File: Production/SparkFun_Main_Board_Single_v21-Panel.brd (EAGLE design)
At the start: 186.9 x 176.3 mm, 510 parts, among them J1 MICROMOD-2222-C, J10 MICRO-SD-PUSH-PUSH-EXT-PIN, J11 Vertical Qwiic Connector, J14 QWIIC_RIGHT_ANGLE, J15 MICROMOD-2222-C, J18 CORTEX_JTAG_DEBUG_MINIMUM_PTH, J2 Vertical Qwiic Connector, J20 MICRO-SD-PUSH-PUSH-EXT-PIN, J21 MICROMOD_FUNCTION_MAIN, J25 Vertical Qwiic Connector, J26 QWIIC_RIGHT_ANGLE, J27 MICROMOD-2222-C, J30 CORTEX_JTAG_DEBUG_MINIMUM_PTH, J32 MICRO-SD-PUSH-PUSH-EXT-PIN, J33 MICROMOD_FUNCTION_MAIN, J37 Vertical Qwiic Connector, J38 QWIIC_RIGHT_ANGLE, J39 MICROMOD-2222-C, J4 QWIIC_RIGHT_ANGLE, J42 CORTEX_JTAG_DEBUG_MINIMUM_PTH, J44 MICRO-SD-PUSH-PUSH-EXT-PIN, J45 MICROMOD_FUNCTION_MAIN, J5 CORTEX_JTAG_DEBUG_MINIMUM_PTH, J6 MICROMOD_FUNCTION_MAIN, Q1 3.1A/30V/105mΩ, Q2 20V/4.2A/52mΩ/1.4W, Q3 3.1A/30V/105mΩ, Q4 20V/4.2A/52mΩ/1.4W, Q5 3.1A/30V/105mΩ, Q6 20V/4.2A/52mΩ/1.4W, Q7 3.1A/30V/105mΩ, Q8 20V/4.2A/52mΩ/1.4W, U1 STG3856QTR, U10 AP7347DQ-33W5-7K-3.3V, U11 MCP73831, U12 AP7361C-33, U13 STG3856QTR, U14 ESD Diode, U15 AP7347DQ-33W5-7K-3.3V, U16 MCP73831, U17 AP7361C-33, U18 STG3856QTR, U19 ESD Diode, U2 MCP73831, U20 AP7347DQ-33W5-7K-3.3V, U3 ESD Diode, U4 AP7347DQ-33W5-7K-3.3V, U5 AP7361C-33, U6 MCP73831, U7 AP7361C-33, U8 STG3856QTR, U9 ESD Diode

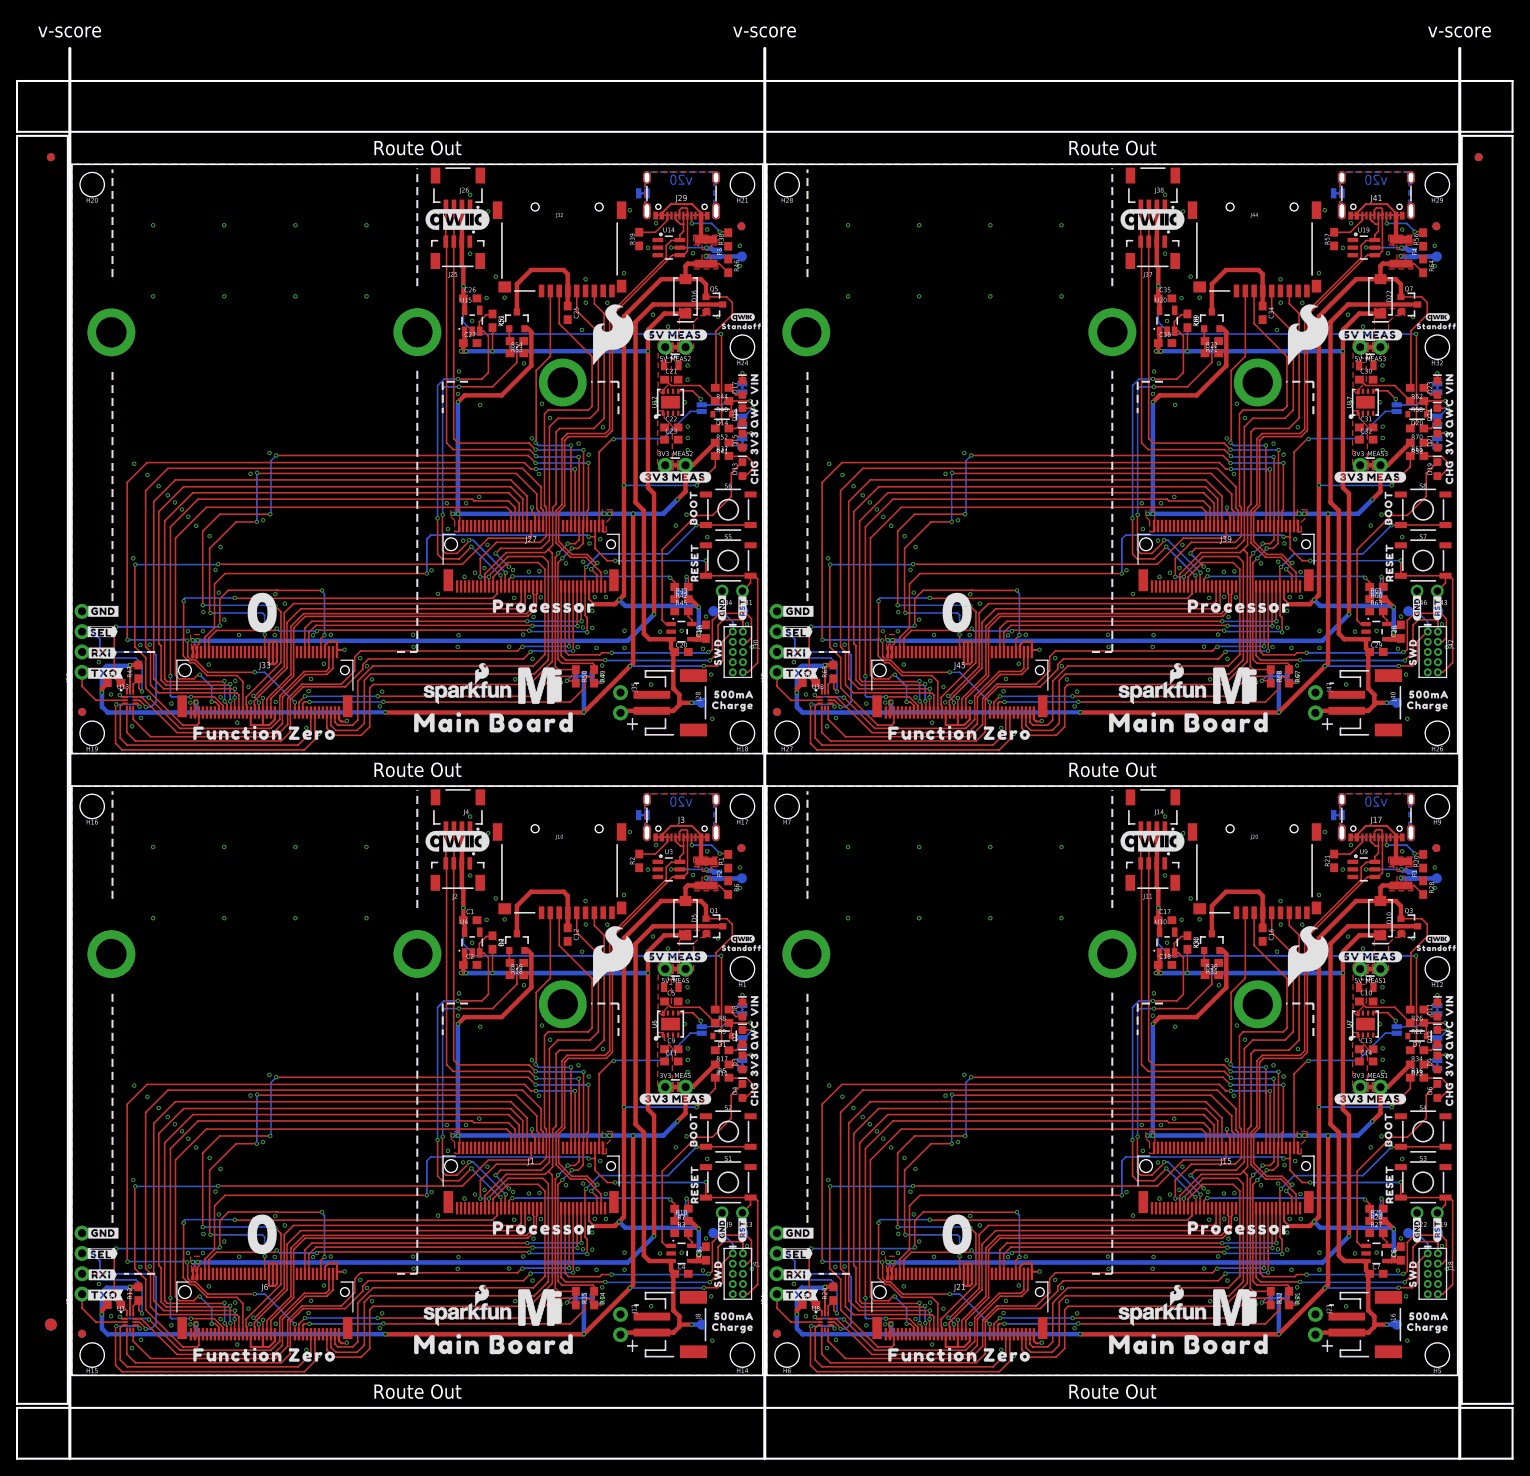
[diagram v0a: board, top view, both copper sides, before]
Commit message: Adds new production files
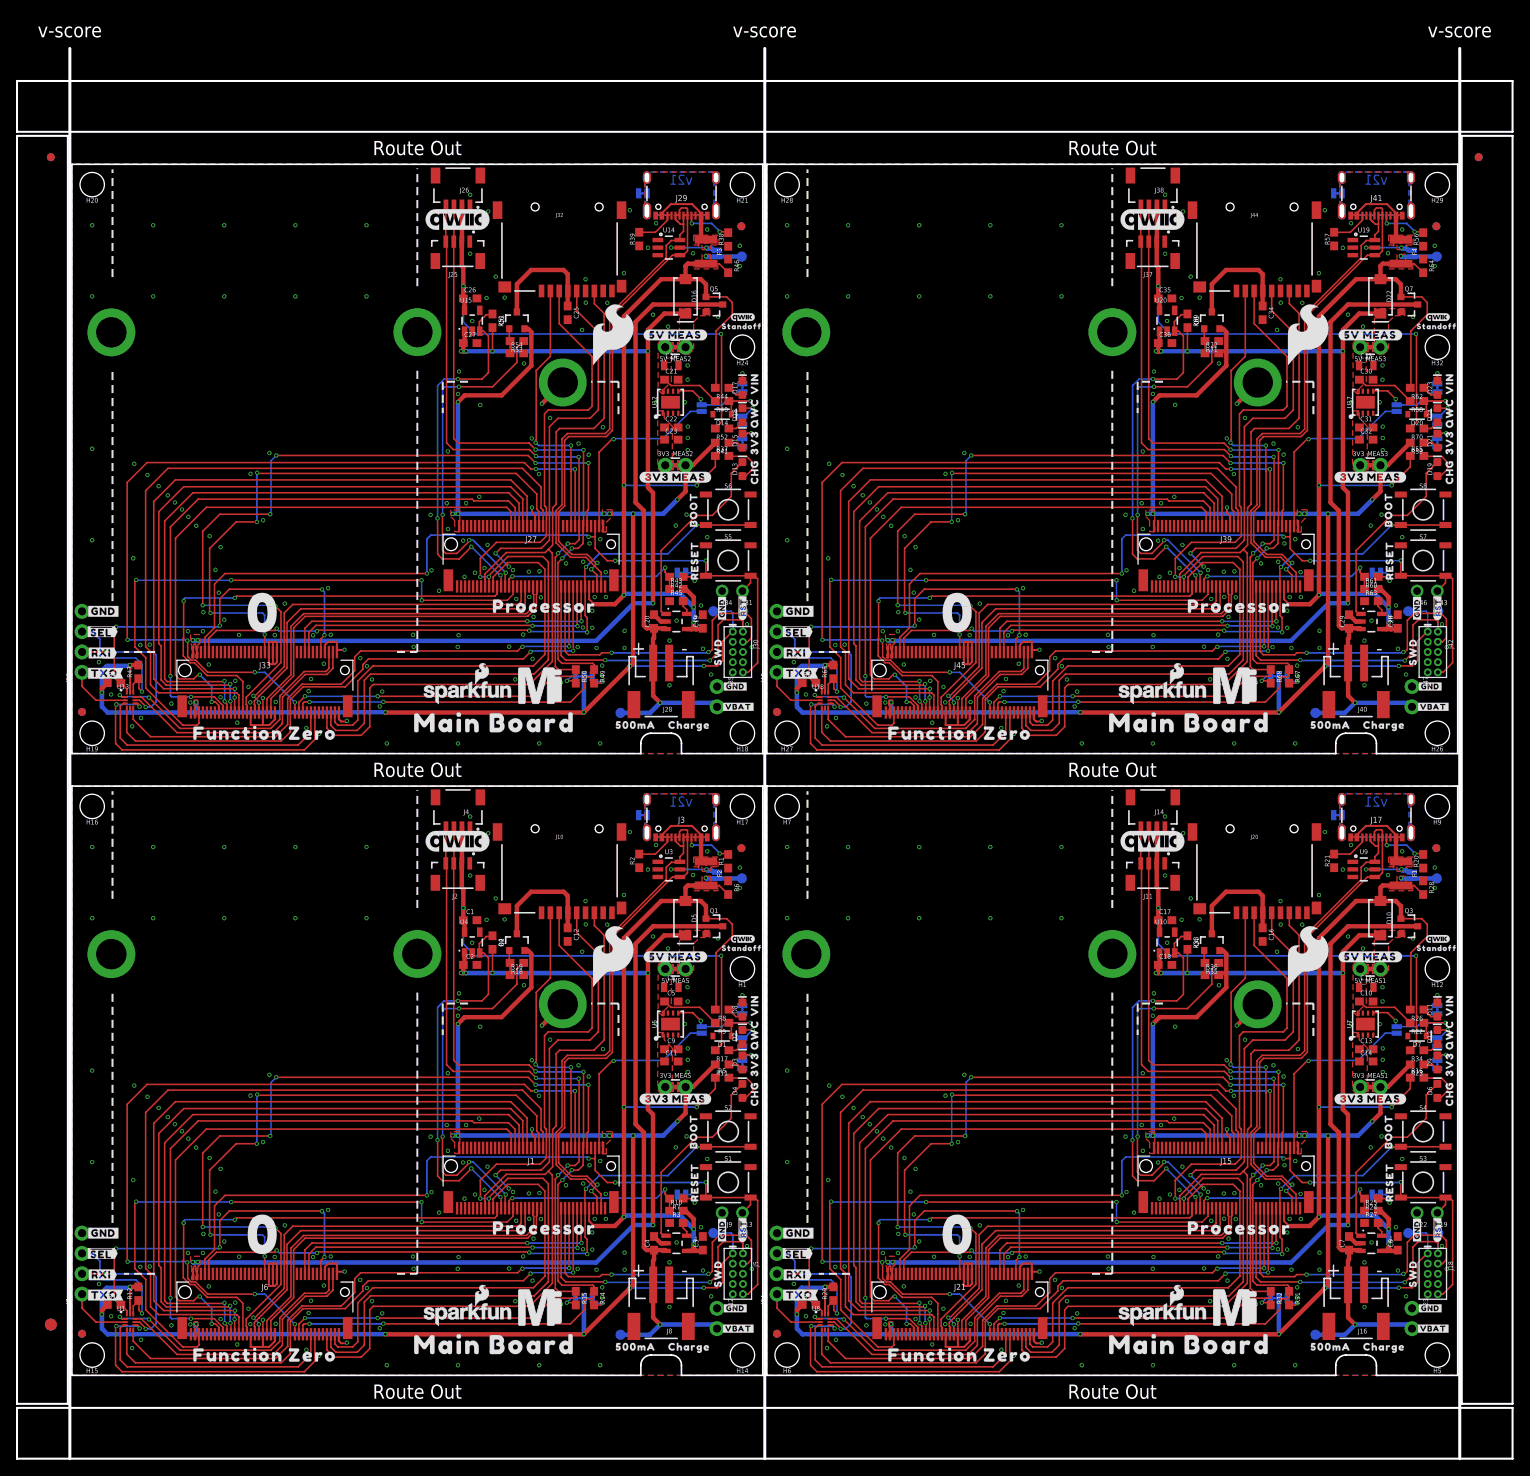
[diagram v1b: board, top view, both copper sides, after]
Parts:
- added U$169: (no value), bot:##SEL##3
- added U$170: (no value), bot:#RXI#4
- added U$171: (no value), bot:#TXO#5
- added U$172: (no value), top:#PTC#15
- added U$173, U$174: (no value), top:#GND#10
- added U$175: (no value), top:##RST##8
- added U$176: (no value), top:#VBAT#9
- U$100: device SparkFun-Aesthetics:SFE_LOGO_FLAME_.3 -> top:MAIN_BOARD5523
- U$101: device top:CHARGE501 -> SparkFun-MicroMod:MICROMOD_LOGO_1
- U$102: device top:#PTC#503 -> SparkFun-Aesthetics:QWIIC_3MM
- U$103: device top:#SHLD#501 -> top:STANDOFF501
- U$104: device top:#3V3_MEAS#6522 -> SparkFun-Aesthetics:SFE_LOGO_FLAME_.3
- U$105: device top:#5V_MEAS#6522 -> top:CHARGE501
- U$106: device top:500MA6520 -> top:#SHLD#501
- U$107: device top:#RST#6521 -> top:#3V3_MEAS#6522
- U$108: device top:#GND#6520 -> top:#5V_MEAS#6522
- U$109: device top:SWD6522 -> top:500MA6520
- U$110: device top:#3V3_EN#23 -> top:SWD6522
- U$111: device top:#3V3_LED#22 -> top:#3V3_EN#23
- U$112: device top:#QWIIC_LED#22 -> top:#3V3_LED#22
- U$113: device top:#DIVIDER#23 -> top:#QWIIC_LED#22
- U$114: device top:#VIN_LED#24 -> top:#DIVIDER#23
- U$115: device top:#I2C#501 -> top:#VIN_LED#24
- U$116: device top:#GND#3 -> top:#I2C#501
- U$118: device top:SWD6522 -> top:#GND#3
- U$119: device SparkFun-Aesthetics:SFE_LOGO_NAME_FLAME_.1 -> top:SWD6522
- U$120: device top:QWC4 -> SparkFun-Aesthetics:SFE_LOGO_NAME_FLAME_.1
- U$121: device top:#TXO#7 -> top:QWC4
- U$122: device top:#RXI#6 -> top:#TXO#7
- U$123: device top:##SEL##5 -> top:#RXI#6
- U$124: device bot:##SEL##3 -> top:##SEL##5
- U$125: device bot:#RXI#4 -> bot:##SEL##3
- U$126: device bot:#TXO#5 -> bot:#RXI#4
- U$127: device top:3V332533 -> bot:#TXO#5
- U$128: device top:VIN32532 -> top:#PTC#15
- U$129: device top:CHG32531 -> top:#GND#10
- U$130: device top:BOOT32541 -> top:#GND#10
- U$131: device top:RESET32540 -> top:##RST##8
- U$132: device top:PROCESSOR525 -> top:#VBAT#9
- U$133: device top:FUNCTION_ZERO520 -> top:3V332533
- U$134: device SparkFun-MicroMod:MICROMOD_MI_LOGO_1 -> top:VIN32532
- U$135: device top:0523 -> top:CHG32531
- U$136: device top:MAIN523 -> top:BOOT32541
- U$137: device top:BOARD524 -> top:RESET32540
- U$138: device top:MAIN_BOARD5523 -> top:PROCESSOR525
- U$139: device SparkFun-MicroMod:MICROMOD_LOGO_1 -> top:FUNCTION_ZERO520
- U$140: device SparkFun-Aesthetics:QWIIC_3MM -> SparkFun-MicroMod:MICROMOD_MI_LOGO_1
- U$141: device top:STANDOFF501 -> top:0523
- U$142: device SparkFun-Aesthetics:SFE_LOGO_FLAME_.3 -> top:MAIN523
- U$143: device top:CHARGE501 -> top:BOARD524
- U$144: device top:#PTC#503 -> top:MAIN_BOARD5523
- U$145: device top:#SHLD#501 -> SparkFun-MicroMod:MICROMOD_LOGO_1
- U$146: device top:#3V3_MEAS#6522 -> SparkFun-Aesthetics:QWIIC_3MM
- U$147: device top:#5V_MEAS#6522 -> top:STANDOFF501
- U$148: device top:500MA6520 -> SparkFun-Aesthetics:SFE_LOGO_FLAME_.3
- U$149: device top:#RST#6521 -> top:CHARGE501
- U$150: device top:#GND#6520 -> top:#SHLD#501
- U$151: device top:SWD6522 -> top:#3V3_MEAS#6522
- U$152: device top:#3V3_EN#23 -> top:#5V_MEAS#6522
- U$153: device top:#3V3_LED#22 -> top:500MA6520
- U$154: device top:#QWIIC_LED#22 -> top:SWD6522
- U$155: device top:#DIVIDER#23 -> top:#3V3_EN#23
- U$156: device top:#VIN_LED#24 -> top:#3V3_LED#22
- U$157: device top:#I2C#501 -> top:#QWIIC_LED#22
- U$158: device top:#GND#3 -> top:#DIVIDER#23
- U$159: device top:#GND#3 -> top:#VIN_LED#24
- U$160: device top:SWD6522 -> top:#I2C#501
- U$161: device SparkFun-Aesthetics:SFE_LOGO_NAME_FLAME_.1 -> top:#GND#3
- U$162: device top:QWC4 -> top:#GND#3
- U$163: device top:#TXO#7 -> top:SWD6522
- U$164: device top:#RXI#6 -> SparkFun-Aesthetics:SFE_LOGO_NAME_FLAME_.1
- U$165: device top:##SEL##5 -> top:QWC4
- U$166: device bot:##SEL##3 -> top:#TXO#7
- U$167: device bot:#RXI#4 -> top:#RXI#6
- U$168: device bot:#TXO#5 -> top:##SEL##5
- U$3: device top:#PTC#503 -> top:#PTC#15
- U$36, U$85: device top:3V332533 -> top:#GND#10
- U$37, U$86: device top:VIN32532 -> top:#GND#10
- U$38, U$87: device top:CHG32531 -> top:##RST##8
- U$39: device top:#RST#6521 -> top:#VBAT#9
- U$40: device top:#GND#6520 -> top:3V332533
- U$41: device top:BOOT32541 -> top:VIN32532
- U$42: device top:RESET32540 -> top:CHG32531
- U$43: device top:PROCESSOR525 -> top:BOOT32541
- U$44: device top:FUNCTION_ZERO520 -> top:RESET32540
- U$45: device SparkFun-MicroMod:MICROMOD_MI_LOGO_1 -> top:PROCESSOR525
- U$46: device top:0523 -> top:FUNCTION_ZERO520
- U$47: device top:MAIN523 -> SparkFun-MicroMod:MICROMOD_MI_LOGO_1
- U$48: device top:BOARD524 -> top:0523
- U$54: device top:MAIN_BOARD5523 -> top:MAIN523
- U$55: device SparkFun-MicroMod:MICROMOD_LOGO_1 -> top:BOARD524
- U$56: device SparkFun-Aesthetics:QWIIC_3MM -> top:MAIN_BOARD5523
- U$57: device top:STANDOFF501 -> SparkFun-MicroMod:MICROMOD_LOGO_1
- U$58: device SparkFun-Aesthetics:SFE_LOGO_FLAME_.3 -> SparkFun-Aesthetics:QWIIC_3MM
- U$59: device top:CHARGE501 -> top:STANDOFF501
- U$60: device top:#PTC#503 -> SparkFun-Aesthetics:SFE_LOGO_FLAME_.3
- U$61: device top:#SHLD#501 -> top:CHARGE501
- U$62: device top:#3V3_MEAS#6522 -> top:#SHLD#501
- U$63: device top:#5V_MEAS#6522 -> top:#3V3_MEAS#6522
- U$64: device top:500MA6520 -> top:#5V_MEAS#6522
- U$65: device top:#RST#6521 -> top:500MA6520
- U$66: device top:#GND#6520 -> top:SWD6522
- U$67: device top:SWD6522 -> top:#3V3_EN#23
- U$68: device top:#3V3_EN#23 -> top:#3V3_LED#22
- U$69: device top:#3V3_LED#22 -> top:#QWIIC_LED#22
- U$70: device top:#QWIIC_LED#22 -> top:#DIVIDER#23
- U$71: device top:#DIVIDER#23 -> top:#VIN_LED#24
- U$72: device top:#VIN_LED#24 -> top:#I2C#501
- U$73: device top:#I2C#501 -> top:#GND#3
- U$75: device top:#GND#3 -> top:SWD6522
- U$76: device top:SWD6522 -> SparkFun-Aesthetics:SFE_LOGO_NAME_FLAME_.1
- U$77: device SparkFun-Aesthetics:SFE_LOGO_NAME_FLAME_.1 -> top:QWC4
- U$78: device top:QWC4 -> top:#TXO#7
- U$79: device top:#TXO#7 -> top:#RXI#6
- U$80: device top:#RXI#6 -> top:##SEL##5
- U$81: device top:##SEL##5 -> bot:##SEL##3
- U$82: device bot:##SEL##3 -> bot:#RXI#4
- U$83: device bot:#RXI#4 -> bot:#TXO#5
- U$84: device bot:#TXO#5 -> top:#PTC#15
- U$88: device top:BOOT32541 -> top:#VBAT#9
- U$89: device top:RESET32540 -> top:3V332533
- U$90: device top:PROCESSOR525 -> top:VIN32532
- U$91: device top:FUNCTION_ZERO520 -> top:CHG32531
- U$92: device SparkFun-MicroMod:MICROMOD_MI_LOGO_1 -> top:BOOT32541
- U$93: device top:0523 -> top:RESET32540
- U$94: device top:MAIN523 -> top:PROCESSOR525
- U$95: device top:BOARD524 -> top:FUNCTION_ZERO520
- U$96: device top:MAIN_BOARD5523 -> SparkFun-MicroMod:MICROMOD_MI_LOGO_1
- U$97: device SparkFun-MicroMod:MICROMOD_LOGO_1 -> top:0523
- U$98: device SparkFun-Aesthetics:QWIIC_3MM -> top:MAIN523
- U$99: device top:STANDOFF501 -> top:BOARD524
- moved U$127 170.6 mm to (4.06, 87.8), flipped to the bottom, turned to 0 degrees
- moved U$88 138.1 mm to (170.2, 5.84), turned to 0 degrees
- moved U$85 137.3 mm to (169.8, 8.38), turned to 0 degrees
- moved U$86 134.3 mm to (168.1, 18.2)
- moved U$87 127.4 mm to (170.7, 18.3)
- moved U$128 95.9 mm to (77.7, 140.2), flipped to the bottom, turned to 0 degrees
- moved U$37 95.2 mm to (81.3, 18.2)
- moved U$36 94.3 mm to (82.9, 8.38), turned to 0 degrees
- moved U$40 93.2 mm to (172.2, 38.9)
- moved U$129 93.2 mm to (82.9, 86.1), turned to 0 degrees
- moved U$84 90.4 mm to (164.6, 62.5)
- moved U$38 90.0 mm to (83.8, 18.3)
- moved U$121 87.5 mm to (85.3, 120.3), turned to 90 degrees
- moved U$78 87.5 mm to (90.9, 10.0), turned to 0 degrees
- moved U$165 86.1 mm to (172.2, 120.3), turned to 90 degrees
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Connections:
- net PWR_EN0: now also J1.47; no longer J1.38
- net PWR_EN1: now also J15.47; no longer J15.38
- net PWR_EN2: now also J27.47; no longer J27.38
- net PWR_EN3: now also J39.47; no longer J39.38
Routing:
- net GND2: track 28.7 -> 34.2 mm, vias 160 -> 169
- net GND3: track 28.7 -> 34.2 mm, vias 160 -> 169
- net GND1: track 28.7 -> 34.2 mm, vias 160 -> 169
- net GND: track 28.7 -> 34.2 mm, vias 160 -> 169
- net PWR_EN2: track 78.2 -> 75.1 mm, vias 2 -> 4
- net PWR_EN1: track 78.2 -> 75.1 mm, vias 2 -> 4
- net PWR_EN3: track 78.2 -> 75.1 mm, vias 2 -> 4
- net PWR_EN0: track 78.2 -> 75.1 mm, vias 2 -> 4
- net N$8: track 26.4 -> 24.8 mm
- net N$43: track 26.4 -> 24.8 mm
- net N$59: track 26.4 -> 24.8 mm
- net N$27: track 26.4 -> 24.8 mm
- net V_BATT3: track 74.2 -> 75.7 mm
- net V_BATT1: track 74.2 -> 75.7 mm
- net V_BATT2: track 74.2 -> 75.7 mm
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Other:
- outline, holes or cut-outs redrawn
- board text added: "v21"
- board text removed: "v20"
